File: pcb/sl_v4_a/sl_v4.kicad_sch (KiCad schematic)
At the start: 49 parts, among them J101 PJ-320D-4A, Q101 BSS138, SW101 SKRTLAE010, SW102 SKRTLAE010, SW103 SKRTLAE010, U101 W25Q16JVSNIQ, U102 RP2040, Y101 ABM8-272-T3

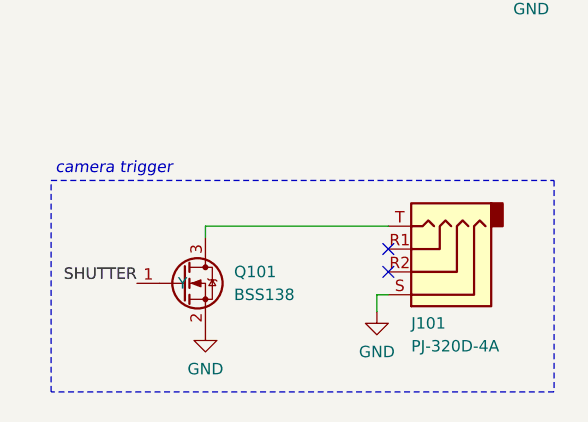
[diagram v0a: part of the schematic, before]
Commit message: remove csv from gitignore, regenerate BOMs and schematics
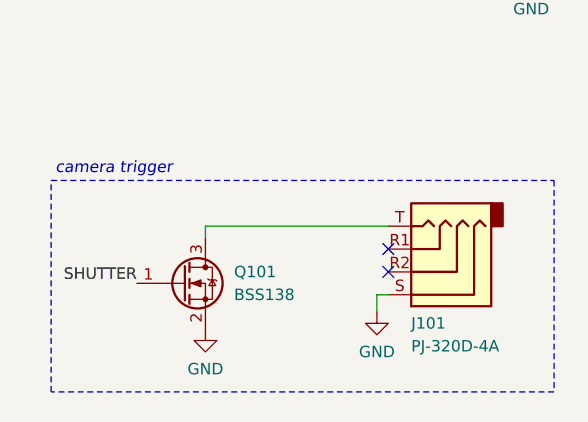
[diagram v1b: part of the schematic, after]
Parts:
- C101, C102, C103, C104, C105, C106, C107, C108, C115, C116: Category iND87204 Critical -> (none); JLCPCB Basic Y -> (none); Non-Critical Y -> (none)
- C109, C110, C111, C112, C113, C114, FB101, Q101, R103, R104, R105, R106, R107, R108, R109: JLCPCB Basic Y -> (none)
